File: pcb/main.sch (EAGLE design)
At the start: 32 parts, among them IC1 74HCT04N, IC2 74HCT04N, IC3 74HCT04N, IC4 74HCT04N

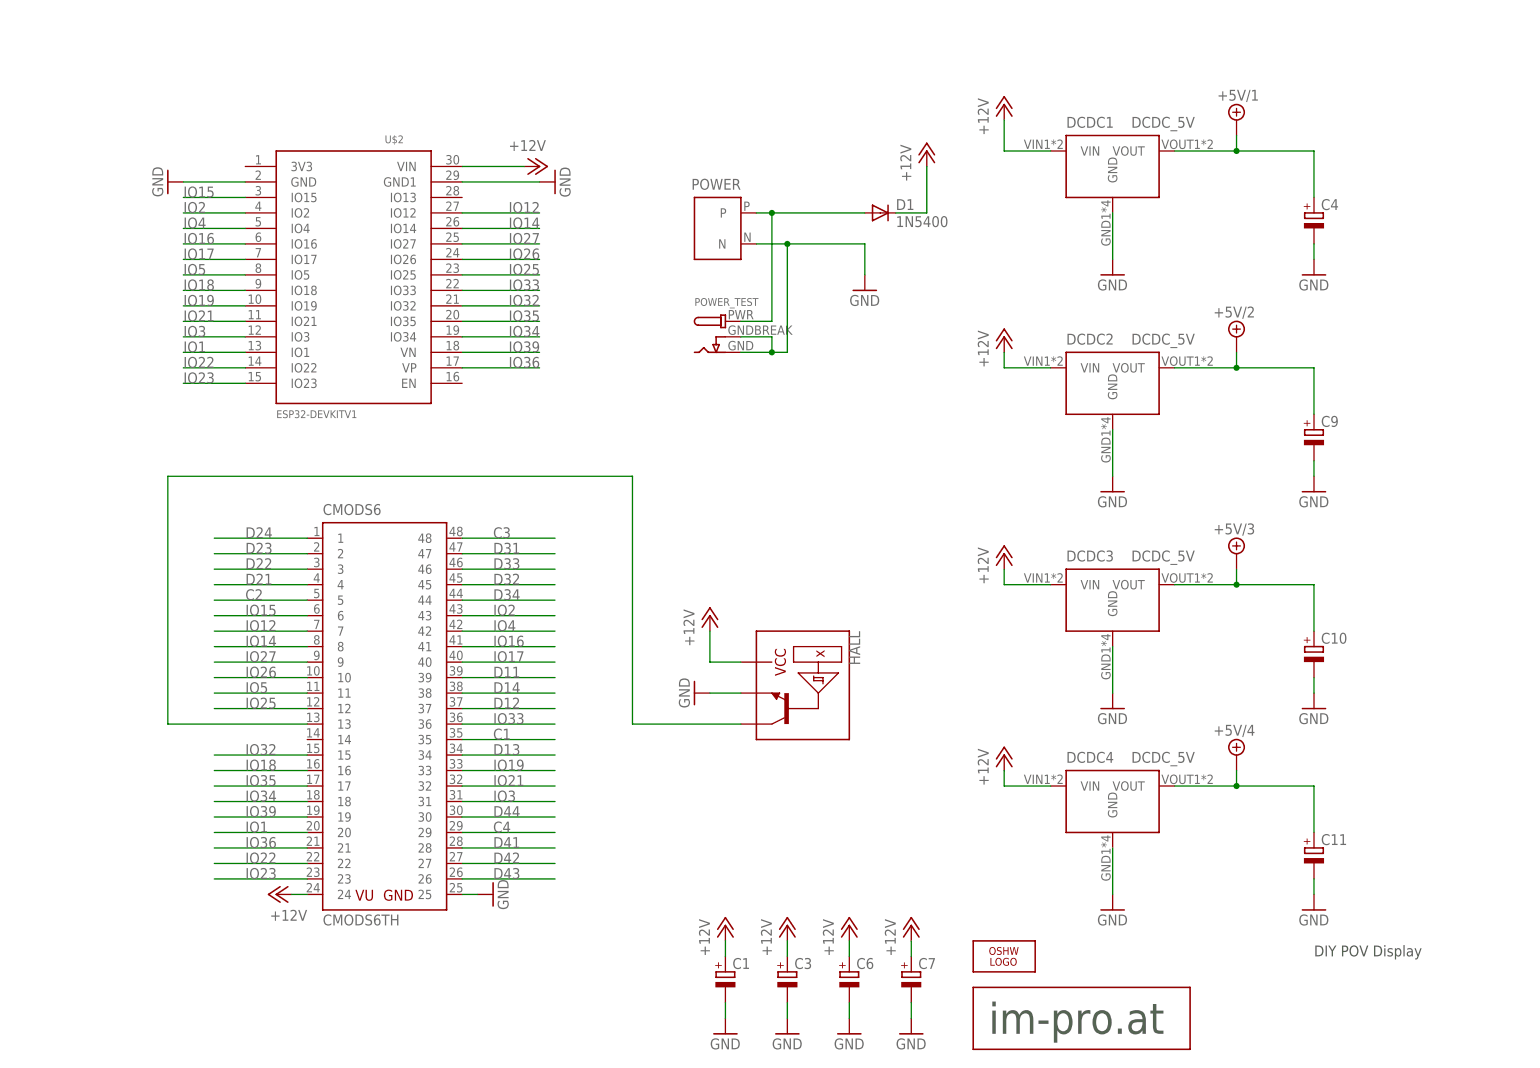
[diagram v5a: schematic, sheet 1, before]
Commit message: finished main pcb layout
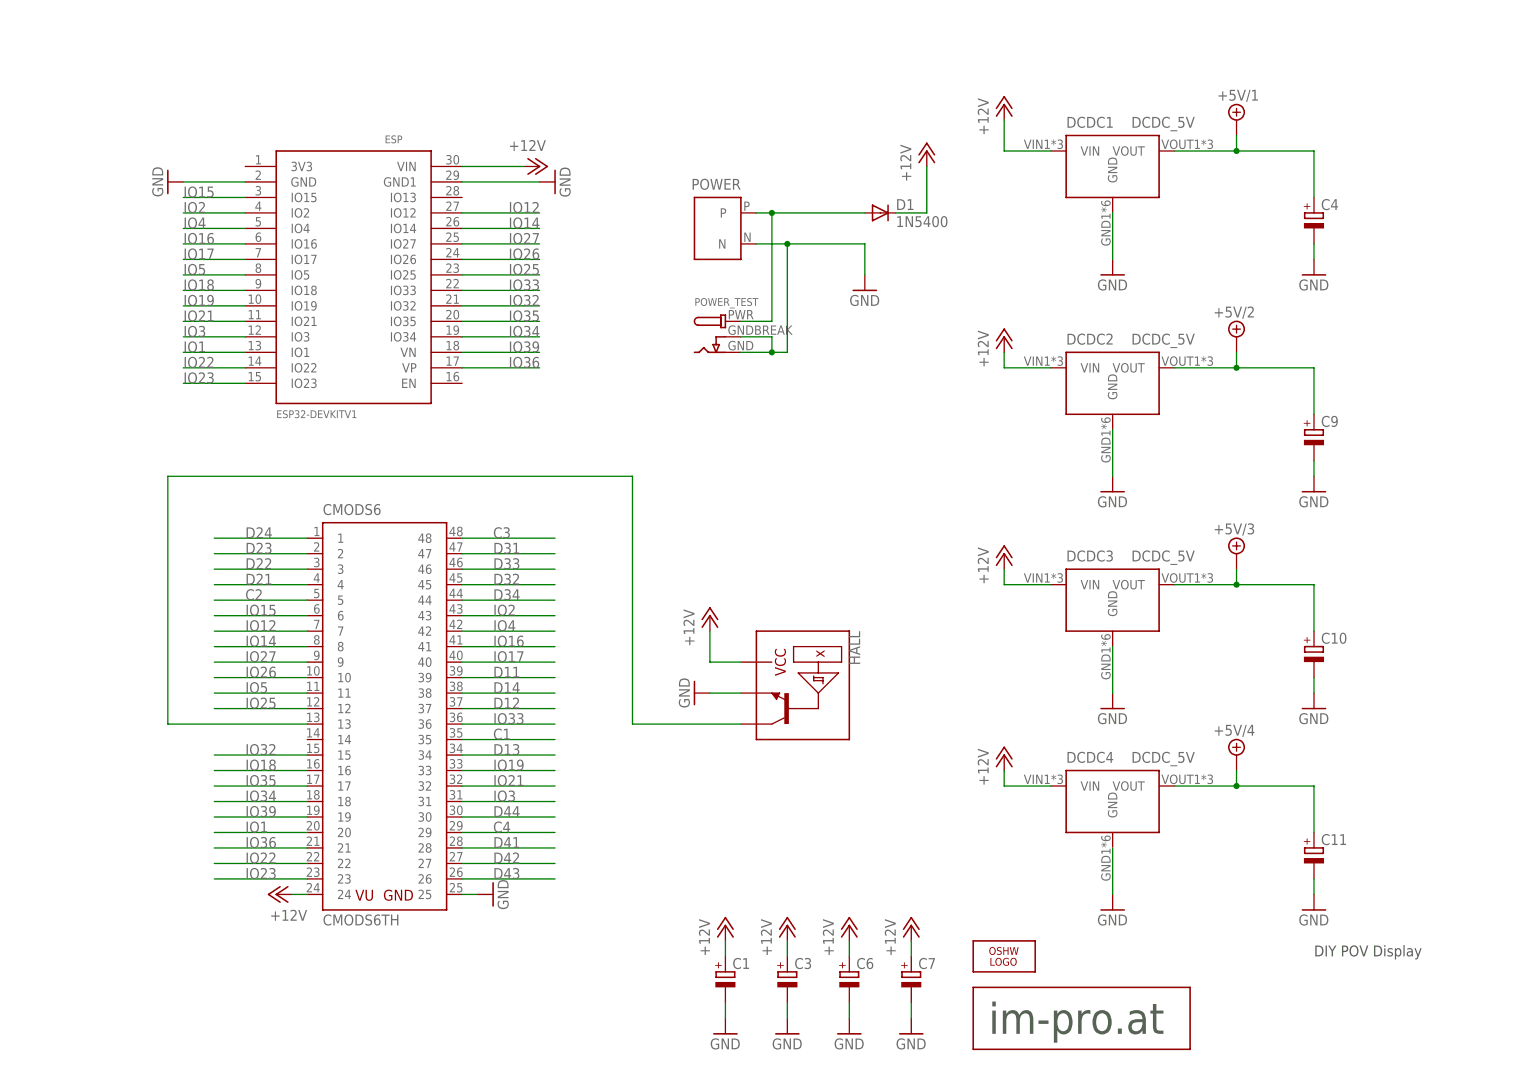
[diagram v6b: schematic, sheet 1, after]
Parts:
- removed U$1: LOGO50MM, im-pro-logo:LOGO50MM
- added ESP: ESP32DEVKITV1, ESP32-DEVKITV1:ESP32DEVKITV1
- U$2: value ESP32DEVKITV1 -> LOGO20MM; device ESP32-DEVKITV1:ESP32DEVKITV1 -> im-pro-logo:LOGO20MM
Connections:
- net +12V: now also ESP.VIN; no longer U$2.VIN
- net GND: now also ESP.GND, ESP.GND1; no longer U$2.GND, U$2.GND1
- net IO1: now also ESP.IO1; no longer U$2.IO1
- net IO12: now also ESP.IO12; no longer U$2.IO12
- net IO14: now also ESP.IO14; no longer U$2.IO14
- net IO15: now also ESP.IO15; no longer U$2.IO15
- net IO16: now also ESP.IO16; no longer U$2.IO16
- net IO17: now also ESP.IO17; no longer U$2.IO17
- net IO18: now also ESP.IO18; no longer U$2.IO18
- net IO19: now also ESP.IO19; no longer U$2.IO19
- net IO2: now also ESP.IO2; no longer U$2.IO2
- net IO21: now also ESP.IO21; no longer U$2.IO21
- net IO22: now also ESP.IO22; no longer U$2.IO22
- net IO23: now also ESP.IO23; no longer U$2.IO23
- net IO25: now also ESP.IO25; no longer U$2.IO25
- net IO26: now also ESP.IO26; no longer U$2.IO26
- net IO27: now also ESP.IO27; no longer U$2.IO27
- net IO3: now also ESP.IO3; no longer U$2.IO3
- net IO32: now also ESP.IO32; no longer U$2.IO32
- net IO33: now also ESP.IO33; no longer U$2.IO33
- net IO34: now also ESP.IO34; no longer U$2.IO34
- net IO35: now also ESP.IO35; no longer U$2.IO35
- net IO36: now also ESP.VP; no longer U$2.VP
- net IO39: now also ESP.VN; no longer U$2.VN
- net IO4: now also ESP.IO4; no longer U$2.IO4
- net IO5: now also ESP.IO5; no longer U$2.IO5

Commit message: layout finished
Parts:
- C1, C10, C11, C3, C4, C6, C7, C9: value (none) -> 220u
- C12, C2, C5, C8: value (none) -> 100n
